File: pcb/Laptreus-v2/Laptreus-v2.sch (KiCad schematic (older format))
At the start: 124 parts, among them IC1 ATMEGA32U4, J1 HRO-TYPE-C-31-M-12, SW1 TAB, SW10 O, SW11 P, SW12 BKSP, SW13 ESC, SW14 A, SW15 S, SW16 D, SW17 F/LOWER, SW18 G, SW19 H, SW2 Q, SW20 J/RAISE, SW21 K, SW22 L, SW23 ;, SW24 \", SW25 SHIFT, SW26 Z, SW27 X, SW28 C, SW29 V, SW3 W, SW30 B, SW31 N, SW32 M, SW33 ,, SW34 ., SW35 /, SW36 ENTER, SW37 HYPER, SW38 CTRL/GRV, SW39 ALT/TAB, SW4 E, SW40 CMD, SW41 SHIFT, SW42 BKSP/LIFT, SW43 ENTER/LIFT, SW44 SPACE, SW45 LEFT, SW46 DOWN, SW47 UP, SW48 RIGHT, SW5 R, SW6 T, SW7 Y, SW8 U, SW9 I, U6 PRTR5V0U2X, Y1 8MHz

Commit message: v2.3 of shapeshifter 4060, also plate
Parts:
- removed L1: YELLOW, Adafruit Feather 32u4 Bluefruit LE:CHIPLED_0805_NOOUTLINE, symbol Adafruit-parts:LED0805_NOOUTLINE
- added J2: Conn_01x04, Connector_JST:JST_SH_SM04B-SRSS-TB_1x04-1MP_P1.00mm_Horizontal, symbol Connector_Generic:Conn_01x04
- added J3, J4: Conn_01x04_Female, Connector_PinHeader_1.00mm:PinHeader_1x04_P1.00mm_Vertical, symbol Connector:Conn_01x04_Female
- added L1: YELLOW, LED_SMD:LED_0603_1608Metric_Castellated, symbol Device:LED
- D1, D10, D11, D12, D13, D14, D15, D16, D17, D18, D19, D2, D20, D21, D22, D23, D24, D25, D26, D27, D28, D29, D3, D30, D31, D32, D33, D34, D35, D36, D37, D38, D39, D4, D40, D41, D42, D43, D44, D45, D46, D47, D48, D5, D6, D7, D8, D9: footprint Laptreus v2 Footprints:Diode-0805 -> Laptreus v2 Footprints:D_SOD-323_With_Adhesive
- F1: footprint Fuse:Fuse_1206_3216Metric_Pad1.42x1.75mm_HandSolder -> Laptreus v2 Footprints:Fuse_1812_4532Metric_With_Adhesive; LCSC Part Number C182310 -> (none); Manufacturer Shenzhen lanson Elec -> Littelfuse; Manufacturer Part Number 12H1200C -> 1812L050PR; Package SMD1206 -> SMD1812
- IC1: footprint Package_QFP:TQFP-44_10x10mm_P0.8mm -> Laptreus v2 Footprints:TQFP-44_10x10mm_P0.8mm
- R1, R10, R11, R12, R13, R8, R9: footprint Laptreus v2 Footprints:0805-NO -> Laptreus v2 Footprints:R_0603_1608Metric_With_Adhesive
- SW2: footprint Laptreus v2 Footprints:Kailh_Socket_With_Diode_No_Diode_Trace -> Laptreus v2 Footprints:Hybrid_Kailh_MX_Choc_Socket_Through_Hole_With_Diode
- SW25: footprint Laptreus v2 Footprints:Hybrid_Kailh_MX_Choc_Socket_Through_Hole_With_Diode -> Laptreus v2 Footprints:Hybrid_Kailh_MX_Choc_Socket_Through_Hole_With_Diode_No_Diode_Trace
- U6: footprint Package_TO_SOT_SMD:SOT-143_Handsoldering -> Laptreus v2 Footprints:SOT-143_With_Adhesive
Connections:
- net LED_STRIP_IN is gone; now on net B7-LED-STRIP: JP1.1
- net +5VRAW: now also J3.1 (Pin_1)
- net D+: now also J3.3 (Pin_3)
- net D-: now also J3.2 (Pin_2)
- net GND: now also J3.4 (Pin_4), L1.1 (K)
- net at R13.1: now also L1.2 (A)
- new net: J2.1 (Pin_1), J4.1 (Pin_1)
- new net: J2.2 (Pin_2), J4.2 (Pin_2)
- new net: J2.3 (Pin_3), J4.3 (Pin_3)
- new net: J2.4 (Pin_4), J4.4 (Pin_4)
- no-connect marks 9 -> 10

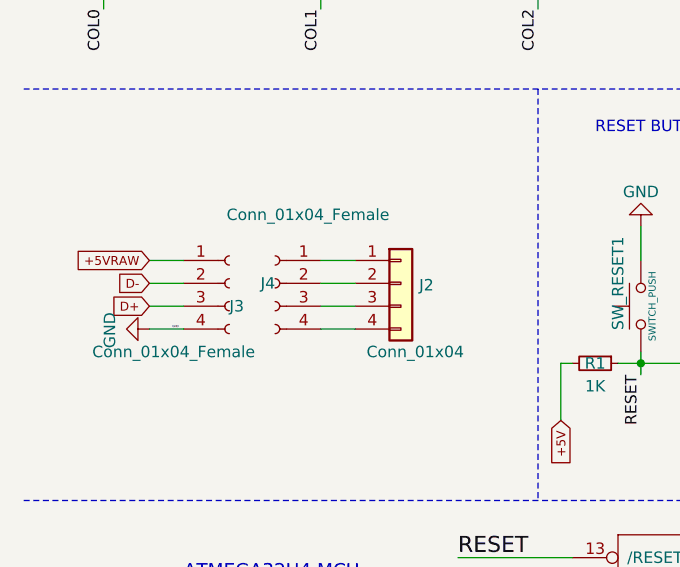
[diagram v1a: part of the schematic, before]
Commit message: Update to remove jst-sh connector
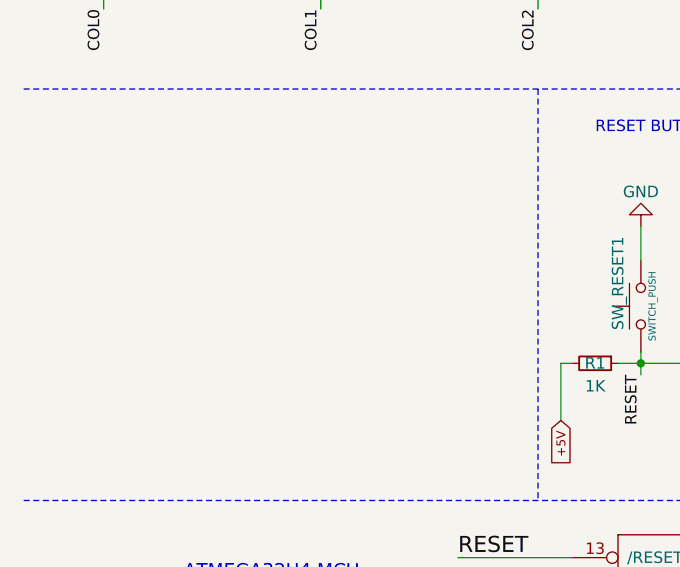
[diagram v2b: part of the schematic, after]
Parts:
- removed J2: Conn_01x04, Connector_JST:JST_SH_SM04B-SRSS-TB_1x04-1MP_P1.00mm_Horizontal, symbol Connector_Generic:Conn_01x04
- removed J3, J4: Conn_01x04_Female, Connector_PinHeader_1.00mm:PinHeader_1x04_P1.00mm_Vertical, symbol Connector:Conn_01x04_Female
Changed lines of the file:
@@
 EESchema Schematic File Version 4
 LIBS:Laptreus-v2-cache
-EELAYER 29 0
+EELAYER 26 0
 EELAYER END
 $Descr A3 11693 16535 portrait
@@
 Text Label 4900 6600 2    39   ~ 0
 B7-LED-STRIP
-Text GLabel 550  4000 0    39   Input ~ 0
-+5VRAW
-Wire Wire Line
-	700  4000 550  4000
-Text GLabel 550  4200 0    39   Input ~ 0
-D+
-Text GLabel 550  4100 0    39   Input ~ 0
-D-
-$Comp
-L Laptreus-v2:GND #PWR02
-U 1 1 5D83B719
-P 550 4300
-F 0 "#PWR02" H 550 4050 50  0001 C CNN
-F 1 "GND" H 555 4127 50  0000 C CNN
-F 2 "" H 550 4300 50  0001 C CNN
-F 3 "" H 550 4300 50  0001 C CNN
-	1    550  4300
-	0    1    1    0
-$EndComp
-Wire Wire Line
-	550  4100 700  4100
-Wire Wire Line
-	700  4200 550  4200
-Wire Wire Line
-	550  4300 700  4300
-Text Label 650  4300 0    9    ~ 0
-GND
 NoConn ~ 4300 6800
 $Comp
@@
 Wire Wire Line
 	5800 6400 6000 6400
-$Comp
-L Connector:Conn_01x04_Female J3
-U 1 1 5DB1E1D9
-P 900 4100
-F 0 "J3" H 900 4000 50  0000 L CNN
-F 1 "Conn_01x04_Female" H 300 3800 50  0000 L CNN
-F 2 "Connector_PinHeader_1.00mm:PinHeader_1x04_P1.00mm_Vertical" H 900 4100 50  0001 C CNN
-F 3 "~" H 900 4100 50  0001 C CNN
-	1    900  4100
-	1    0    0    -1
-$EndComp
-$Comp
-L Connector:Conn_01x04_Female J4
-U 1 1 5E110584
-P 1100 4100
-F 0 "J4" H 1100 4100 50  0000 L CNN
-F 1 "Conn_01x04_Female" H 600 4400 50  0000 L CNN
-F 2 "Connector_PinHeader_1.00mm:PinHeader_1x04_P1.00mm_Vertical" H 1100 4100 50  0001 C CNN
-F 3 "~" H 1100 4100 50  0001 C CNN
-	1    1100 4100
-	-1   0    0    -1
-$EndComp
-$Comp
-L Connector_Generic:Conn_01x04 J2
-U 1 1 5D7A980E
-P 1650 4100
-F 0 "J2" H 1730 4092 50  0000 L CNN
-F 1 "Conn_01x04" H 1500 3800 50  0000 L CNN
-F 2 "Connector_JST:JST_SH_SM04B-SRSS-TB_1x04-1MP_P1.00mm_Horizontal" H 1650 4100 50  0001 C CNN
-F 3 "~" H 1650 4100 50  0001 C CNN
-	1    1650 4100
-	1    0    0    -1
-$EndComp
-Wire Wire Line
-	1300 4000 1450 4000
-Wire Wire Line
-	1300 4100 1450 4100
-Wire Wire Line
-	1300 4200 1450 4200
-Wire Wire Line
-	1300 4300 1450 4300
 $EndSCHEMATC
